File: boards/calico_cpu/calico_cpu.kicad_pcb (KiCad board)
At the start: 2 copper layers, 295.9 x 167 mm, 250 parts, among them J1 Conn_01x06, J2 Conn_02x10_Top_Bottom, J3 Conn_02x06_Top_Bottom, J4 Conn_02x06_Top_Bottom, U1 74HC161, U10 74HC161, U11 74HC138, U12 74HC153, U13 74HC153, U14 74HC153, U15 74HC153, U16 74HC153, U17 74HC153, U18 74HC153, U19 74HC153, U2 74HC161, U20 74HC08, U21 74HC08, U22 74HC283, U23 74HC283, U24 74HC00, U25 74HC00, U26 74HC153, U27 74HC153, U28 74HC153, U29 74HC153, U3 74HC161, U30 74HC157, U31 74HC157, U32 74HC283, U33 74HC283, U34 74HC157, U35 74HC157, U36 74HC08, U37 74HC283, U38 74HC283, U39 74HC08, U4 74HC161, U40 74HC153, U41 74HC153, U42 74HC153, U43 74HC153, U44 74HC157, U45 74HC157, U46 74HC02, U47 74HC21, U48 74HC00, U49 74HC161, U5 74HC161, U50 74HC161, U51 74HC161, U52 74HC161, U53 74HC161, U54 74HC161, U55 74HC161, U56 74HC161, U57 74HC138, U58 74HC126, U59 74HC126, U6 74HC161, U60 74HC126, U61 74HC126, U62 74HC273, U63 74HC273, U64 74HC153, U65 74HC153, U66 74HC153, U67 74HC153, U7 74HC161, U8 74HC161, U9 74HC161

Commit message: calico_cpu: reduce board size
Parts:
- moved C1 109.4 mm to (111.5, 170.2)
- moved C11 109.4 mm to (111.5, 163.2)
- moved C2 109.4 mm to (111.5, 182.9)
- moved U1 109.4 mm to (110.5, 180.3)
- moved U2 109.4 mm to (110.5, 193.0)
- moved U11 109.4 mm to (110.5, 167.6)
- moved J1 50.0 mm to (91.4, 149.9)
- moved J2 50.0 mm to (91.4, 99.1)
- moved C49 1.27 mm to (293.1, 62.2)
- moved C50 1.27 mm to (293.1, 74.9)
- moved C51 1.27 mm to (293.1, 87.6)
- moved C52 1.27 mm to (293.1, 99.7)
- moved C53 1.27 mm to (293.1, 138.4)
- moved C54 1.27 mm to (293.1, 151.1)
- moved C55 1.27 mm to (293.1, 163.8)
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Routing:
- net /inst_fetch/dest3: track 332.1 -> 218.0 mm
- net /inst_fetch/dest2: track 335.4 -> 228.4 mm
- net /inst_fetch/dest1: track 309.0 -> 209.9 mm
- net /inst_fetch/dest7: track 303.6 -> 209.9 mm, vias 4 -> 2
- net /regs/rdw: track 134.5 -> 42.6 mm
- net /inst_fetch/dest0: track 327.3 -> 235.9 mm
- net /inst_fetch/jump: track 287.4 -> 197.8 mm, vias 1 -> 0
- net /ctl_logic/inst7: track 207.6 -> 295.5 mm
- net /ctl_logic/inst6: track 217.6 -> 304.3 mm, vias 3 -> 2
- net /inst_fetch/dest6: track 326.4 -> 240.5 mm, vias 3 -> 1
- net /inst_fetch/reset: track 733.8 -> 649.1 mm, vias 5 -> 7
- net /inst_fetch/clk: track 761.6 -> 679.3 mm, vias 10 -> 11
- net /inst_fetch/dest5: track 300.5 -> 222.4 mm, vias 3 -> 1
- net /inst_fetch/pc0: track 326.1 -> 402.5 mm
- net /inst_fetch/pc1: track 336.7 -> 412.7 mm
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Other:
- board size 295.9 x 167 mm -> 274.3 x 167 mm

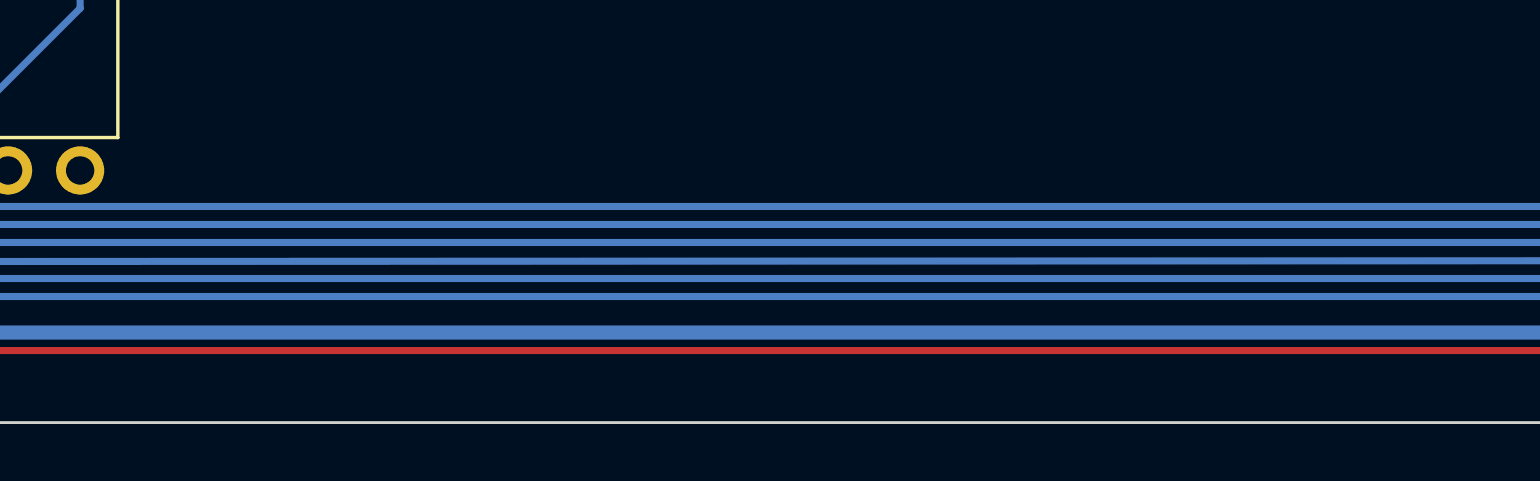
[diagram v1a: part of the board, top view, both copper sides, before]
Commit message: calico_cpu: add origin, name, and drawing area
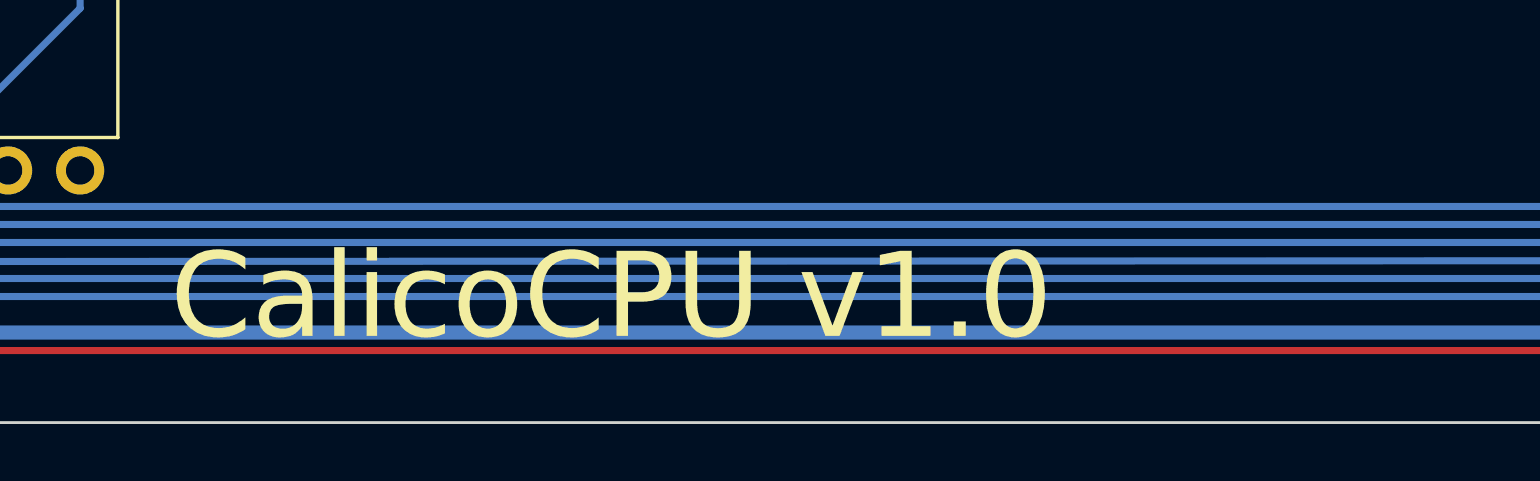
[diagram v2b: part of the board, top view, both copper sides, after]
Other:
- board text added: "CalicoCPU v1.0"
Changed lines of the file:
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@@
   (setup
     (pad_to_mask_clearance 0)
+    (aux_axis_origin 81.28 201.93)
     (pcbplotparams
       (layerselection 0x00010fc_ffffffff)
@@
       (effects (font (size 1 1) (thickness 0.15)))
     )
-    (fp_text value "74HC138" (at 3.81 22.65 90) (layer "F.Fab")
+    (fp_text value "74HC138" (at 3.81 13.97 180) (layer "F.Fab")
       (effects (font (size 1 1) (thickness 0.15)))
     )
@@
       (effects (font (size 1 1) (thickness 0.15)))
     )
-    (fp_text value "74HC161" (at 3.81 22.65 90) (layer "F.Fab")
+    (fp_text value "74HC161" (at 3.81 13.97 180) (layer "F.Fab")
       (effects (font (size 1 1) (thickness 0.15)))
     )
@@
       (effects (font (size 1 1) (thickness 0.15)))
     )
-    (fp_text value "74HC161" (at 3.81 22.65 90) (layer "F.Fab")
+    (fp_text value "74HC161" (at 3.81 13.97 180) (layer "F.Fab")
       (effects (font (size 1 1) (thickness 0.15)))
     )
@@
   (gr_rect (start 324.866 52.07) (end 331.47 67.31) (layer "F.SilkS") (width 0.15) (fill none))
   (gr_line (start 331.47 62.23) (end 324.866 62.23) (layer "F.SilkS") (width 0.15))
+  (gr_rect (start 131.445 153.035) (end 200.025 194.31) (layer "Dwgs.User") (width 0.15) (fill none))
   (gr_rect (start 81.28 34.925) (end 355.6 201.93) (layer "Edge.Cuts") (width 0.1) (fill none))
   (gr_text "5" (at 329.565 55.88) (layer "F.SilkS")
@@
     (effects (font (size 1.5 1.5) (thickness 0.2)))
   )
+  (gr_text "CalicoCPU v1.0" (at 131.445 197.485) (layer "F.SilkS")
+    (effects (font (size 3 3) (thickness 0.45)) (justify left))
+  )
   (gr_text "A" (at 134.62 67.945) (layer "F.SilkS")
     (effects (font (size 3 3) (thickness 0.45)))
@@
   )
   (dimension (type aligned) (layer "Dwgs.User")
+    (pts (xy 131.445 152.4) (xy 200.025 152.4))
+    (height -0.635)
+    (gr_text "68.5800 mm" (at 165.735 150.615) (layer "Dwgs.User")
+      (effects (font (size 1 1) (thickness 0.15)))
+    )
+    (format (units 3) (units_format 1) (precision 4))
+    (style (thickness 0.15) (arrow_length 1.27) (text_position_mode 0) (extension_height 0.58642) (extension_offset 0.5) keep_text_aligned)
+  )
+  (dimension (type aligned) (layer "Dwgs.User")
+    (pts (xy 200.66 153.035) (xy 200.66 194.31))
+    (height -0.635)
+    (gr_text "41.2750 mm" (at 202.565 173.6725 90) (layer "Dwgs.User")
+      (effects (font (size 1 1) (thickness 0.15)))
+    )
+    (format (units 3) (units_format 1) (precision 4))
+    (style (thickness 0.15) (arrow_length 1.27) (text_position_mode 2) (extension_height 0.58642) (extension_offset 0.5) keep_text_aligned)
+  )
+  (dimension (type aligned) (layer "Dwgs.User")
